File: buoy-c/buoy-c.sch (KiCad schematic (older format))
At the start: 98 parts, among them J1 UJ31-CH-G2-SMT-TR, J10 Conn_01x10_Male, J11 TERM-BLK-2P, J12 TERM-BLK-2P, J13 Conn_01x05_Male, J2 BAT-HLD-001-THM, J3 TERM-BLK-2P, J4 U.FL-R-SMT-1_10_, J5 BH-18650-PC, J6 Conn_01x03_Male, J7 TERM-BLK-2P, J8 Conn_01x03_Male, J9 U.FL-R-SMT-1_10_, Q1 MMBT2222LT1G, Q2 MMBT2222LT1G, Q3 MMBT2222LT1G, U1 ATGM332D-5N31, U10 LTC2954ITS8-1#TRPBF, U2 LTC3113EFE#TRPBF, U3 TP4056, U4 ESP32-WROOM-32D, U5 FT260S-U, U6 TPS61030PWPR, U7 RFM95W-915S2, U8 DS3231M+TRL, U9 ADXL343-EVAL

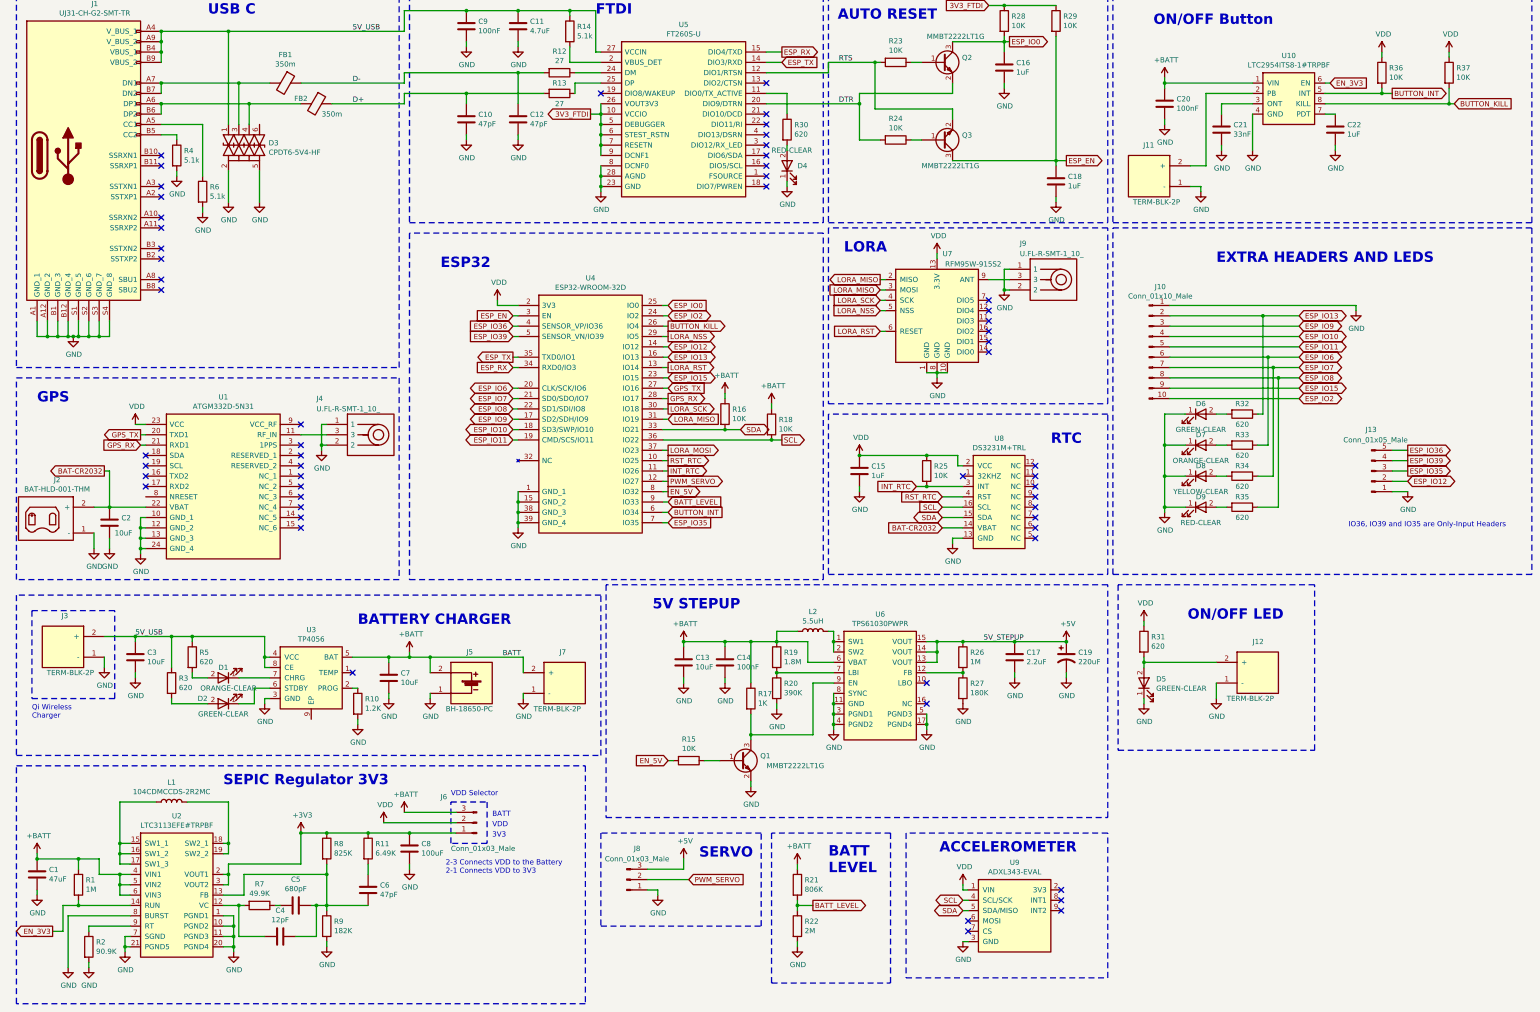
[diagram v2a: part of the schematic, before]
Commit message: Placed components in the PCB
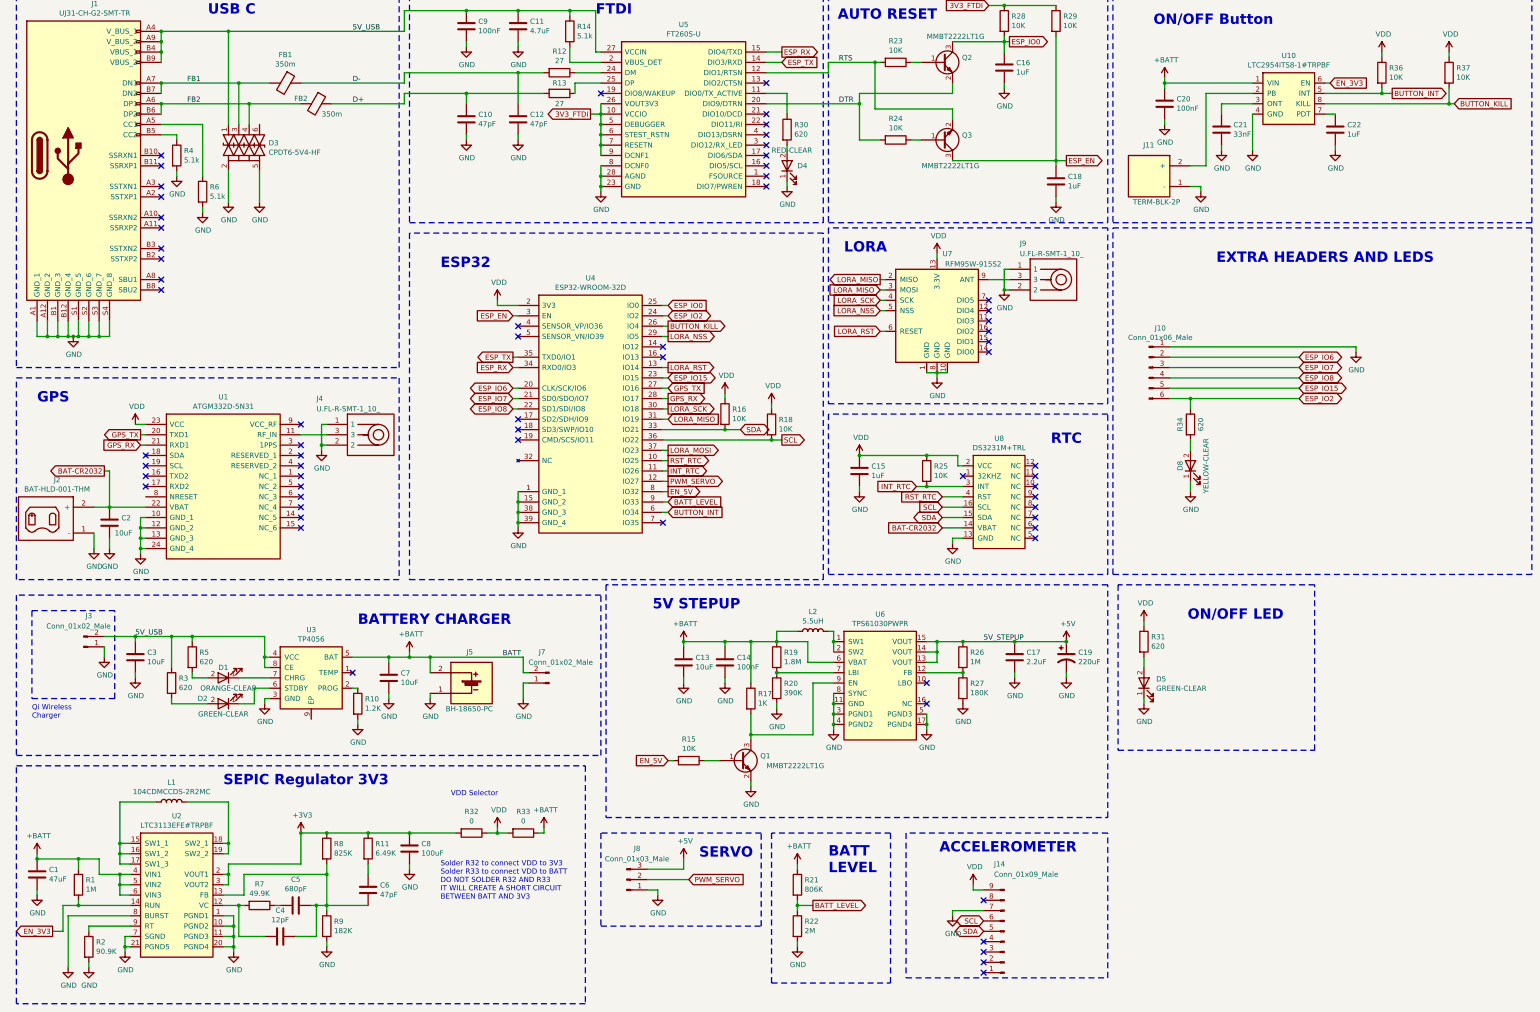
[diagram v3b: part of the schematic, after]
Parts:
- removed D6: GREEN-CLEAR, LED_SMD:LED_0805_2012Metric, symbol LED-GREEN-CLEAR-0805:GREEN-CLEAR
- removed D7: ORANGE-CLEAR, LED_SMD:LED_0805_2012Metric, symbol LED-ORANGE-CLEAR-0805:ORANGE-CLEAR
- removed D9: RED-CLEAR, LED_SMD:LED_0805_2012Metric, symbol LED-RED-CLEAR-0805:RED-CLEAR
- removed J10: Conn_01x10_Male, Connector_PinHeader_2.54mm:PinHeader_1x10_P2.54mm_Vertical, symbol Connector:Conn_01x10_Male
- removed J12, J3, J7: TERM-BLK-2P, TerminalBlock:TerminalBlock_bornier-2_P5.08mm, symbol TERMINAL-BLOCK-2P-508:TERM-BLK-2P
- removed J13: Conn_01x05_Male, Connector_PinHeader_2.54mm:PinHeader_1x05_P2.54mm_Vertical, symbol Connector:Conn_01x05_Male
- removed J6: Conn_01x03_Male, Connector_PinHeader_2.54mm:PinHeader_1x03_P2.54mm_Vertical, symbol Connector:Conn_01x03_Male
- removed R32, R33, R35: 620, Resistor_SMD:R_0805_2012Metric, symbol R-620-0805:620
- removed U9: ADXL343-EVAL, ADXL343-EVAL:ADXL343-EVAL, symbol ADXL343-EVAL:ADXL343-EVAL
- added J10: Conn_01x06_Male, Connector_PinHeader_2.54mm:PinHeader_1x06_P2.54mm_Vertical, symbol Connector:Conn_01x06_Male
- added J14: Conn_01x09_Male, Connector_PinHeader_2.54mm:PinHeader_1x09_P2.54mm_Vertical, symbol Connector:Conn_01x09_Male
- added J3, J7: Conn_01x02_Male, Connector_PinHeader_2.54mm:PinHeader_1x02_P2.54mm_Vertical, symbol Connector:Conn_01x02_Male
- added R32, R33: 0, Resistor_SMD:R_0805_2012Metric, symbol R-0-0805:0
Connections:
- net +3V3: now also R32.2
- net +BATT: now also J7.2 (Pin_2), R33.1; no longer R16.1, R18.1
- net 5V_USB: now also J3.2 (Pin_2)
- net ESP_IO15: now also J10.5 (Pin_5)
- net ESP_IO2: now also R34.1, J10.6 (Pin_6)
- net ESP_IO6: now also J10.2 (Pin_2)
- net ESP_IO7: now also J10.3 (Pin_3); no longer R34.1
- net ESP_IO8: now also J10.4 (Pin_4)
- net GND: now also J10.1 (Pin_1), J14.7 (Pin_7), J3.1 (Pin_1), J7.1 (Pin_1)
- net SCL: now also J14.6 (Pin_6)
- net SDA: now also J14.5 (Pin_5)
- net VDD: now also R16.1, R18.1, J14.9 (Pin_9), R32.1, R33.2
- net FB2: now reaches D3.4, FB2.2, J1.A6 (DP1), J1.B6 (DP2)
- net FB1: now reaches D3.3, FB1.2, J1.A7 (DN1), J1.B7 (DN2)
- net ESP_IO10: no longer names the net of U4.18 (SD3/SWP/IO10)
- net ESP_IO11: no longer names the net of U4.19 (CMD/SCS/IO11)
- net ESP_IO12: no longer names the net of U4.14 (IO12)
- net ESP_IO13: no longer names the net of U4.16 (IO13)
- net ESP_IO35: no longer names the net of U4.7 (IO35)
- net ESP_IO36: no longer names the net of U4.4 (SENSOR_VP/IO36)
- net ESP_IO39: no longer names the net of U4.5 (SENSOR_VN/IO39)
- net ESP_IO9: no longer names the net of U4.17 (SD2/SDH/IO9)
- no-connect marks 57 -> 65
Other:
- note added: "Solder R32 to connect VDD to 3V3\nSolder R33 to connect VDD to BATT\nDO NOT SOLDER R32 AND R33\nIT WILL CREATE A SHORT CIRCUIT\nBETWEEN BATT AND 3V3"
- note removed: "2-3 Connects VDD to the Battery\n2-1 Connects VDD to 3V3"
- note removed: "3V3"
- note removed: "BATT"
- note removed: "IO36, IO39 and IO35 are Only-Input Headers"
- note removed: "VDD"
- moved on the sheet: D8, R34

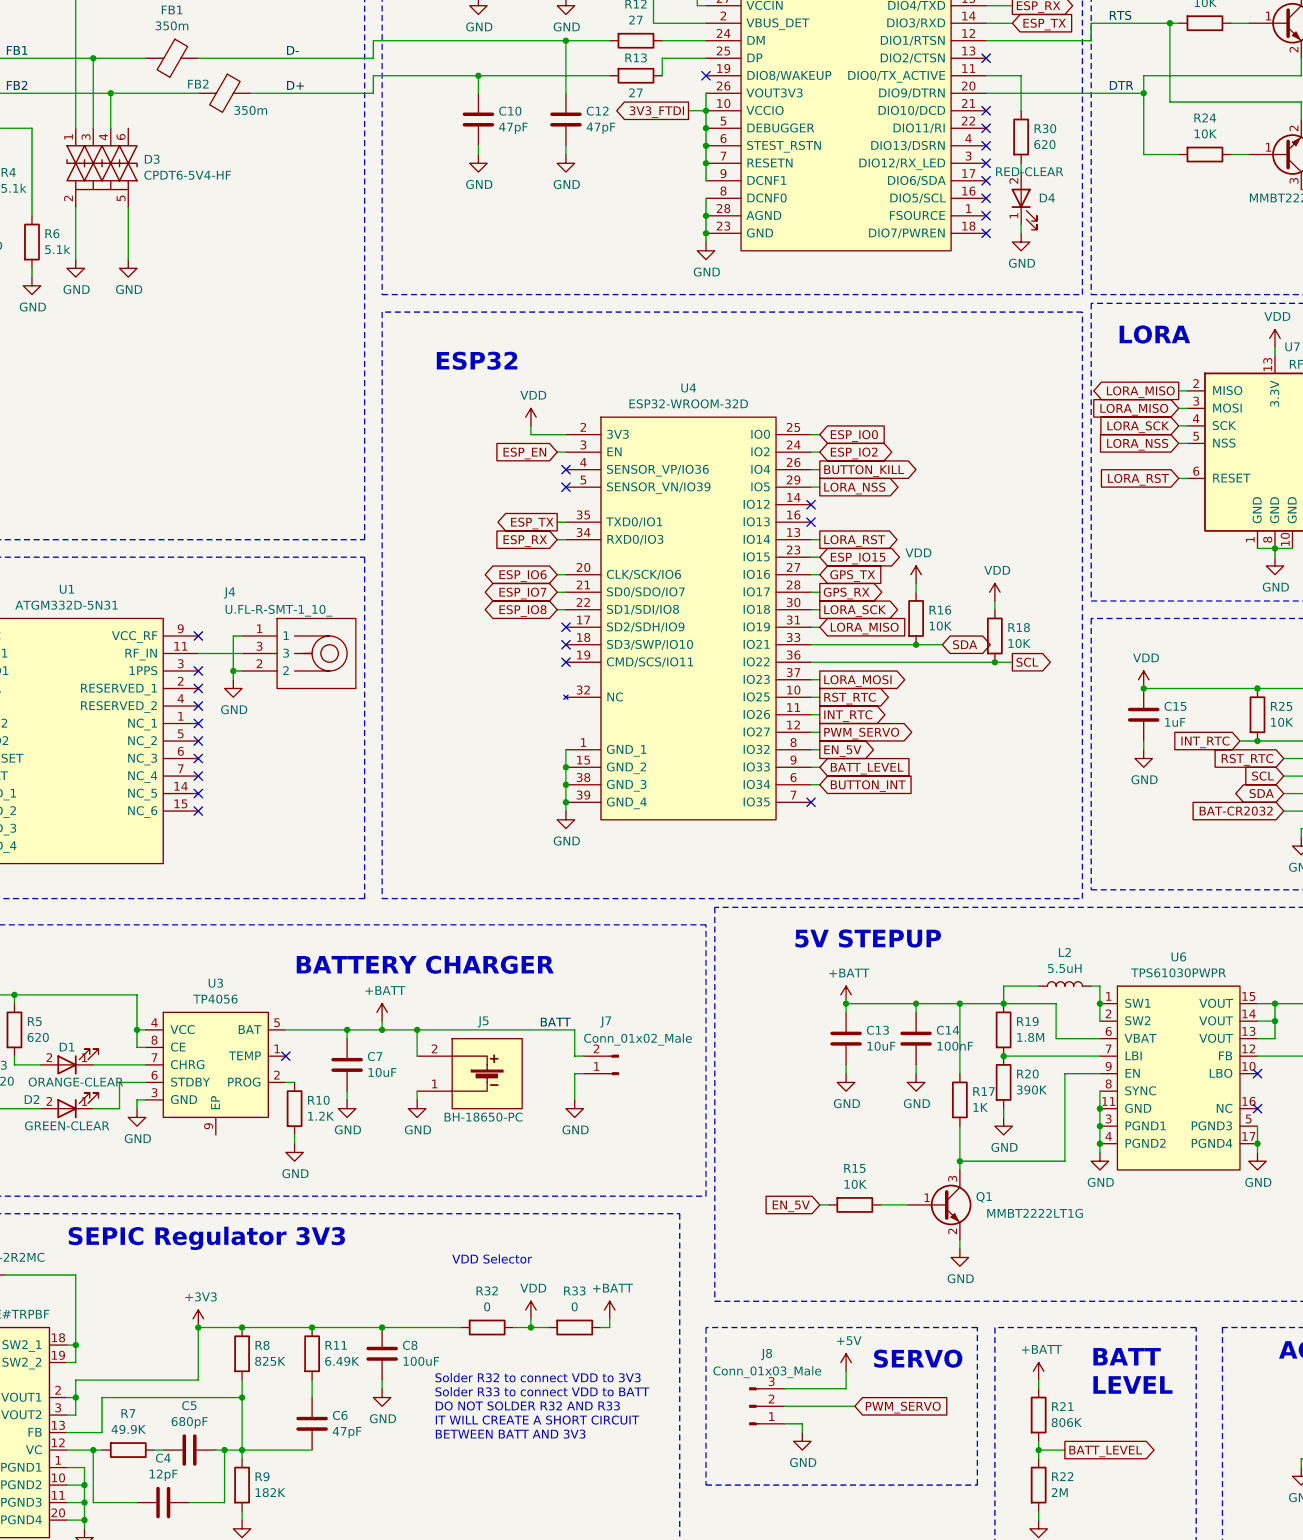
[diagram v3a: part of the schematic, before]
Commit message: Finished routing, solved unconnected
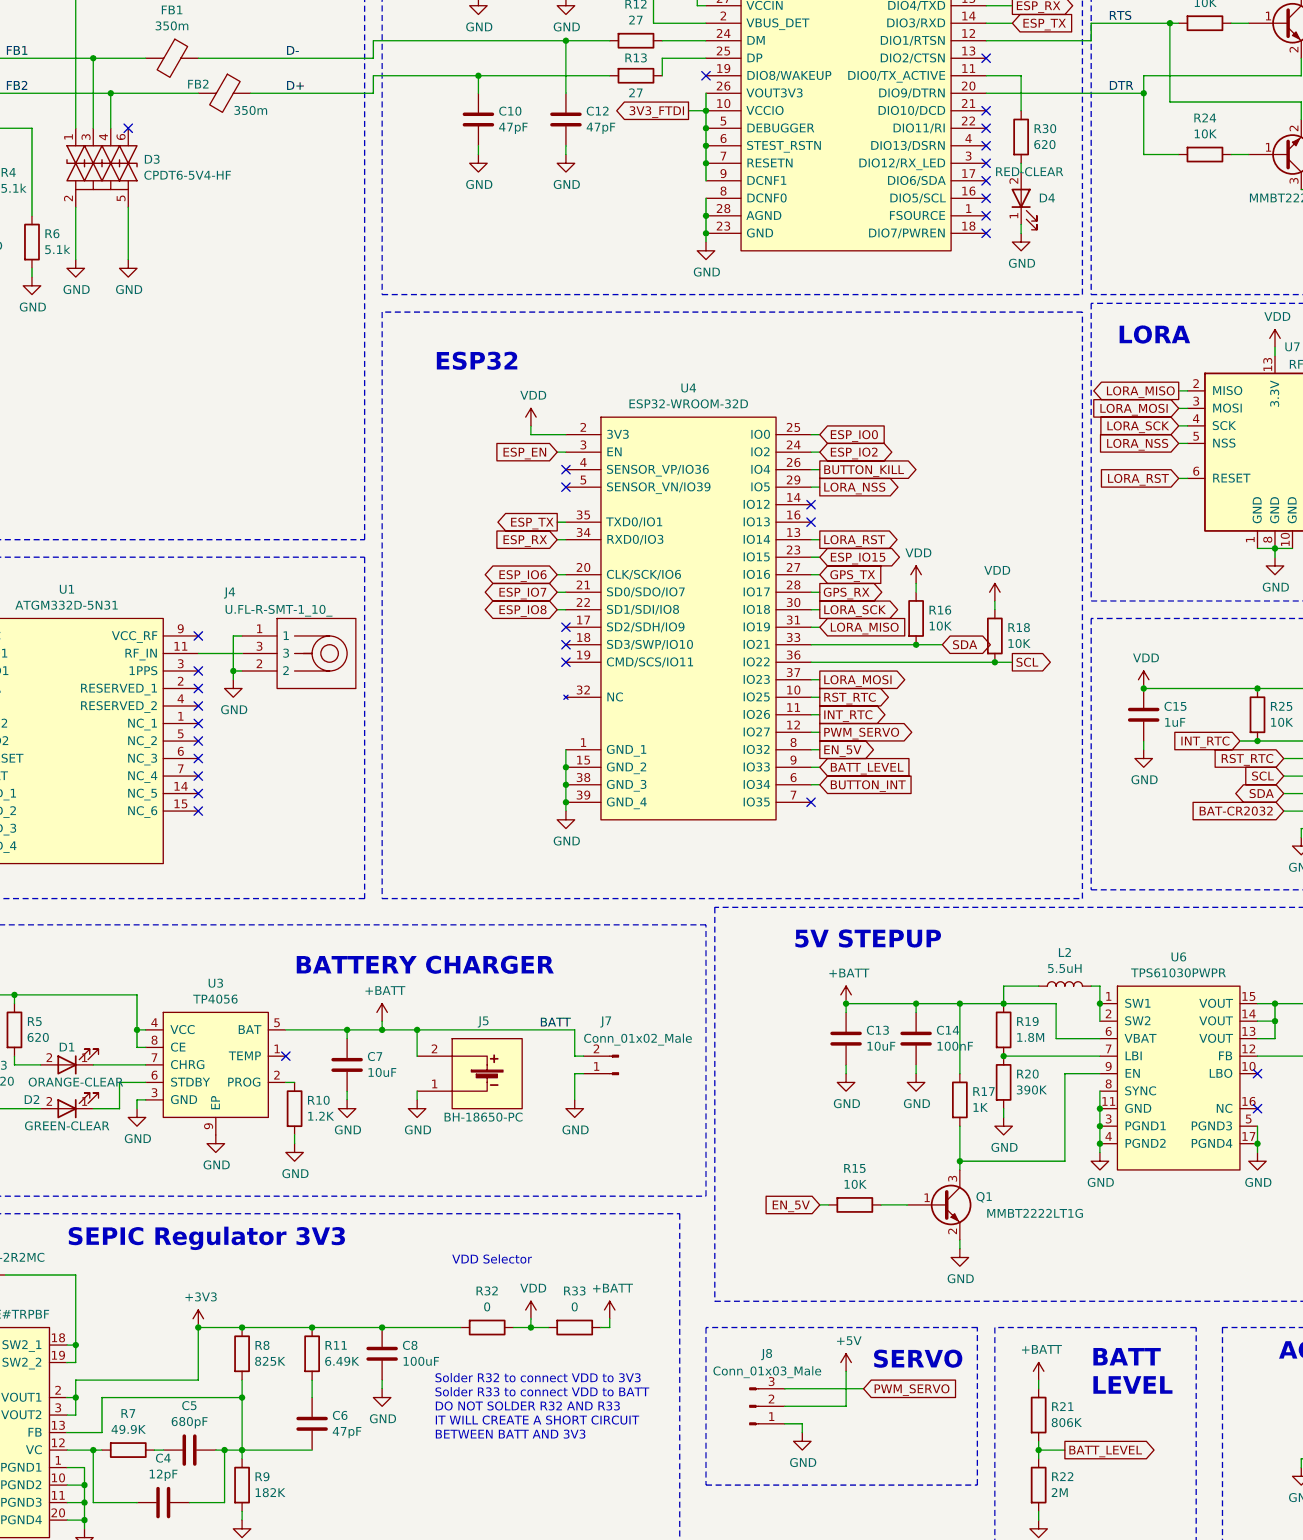
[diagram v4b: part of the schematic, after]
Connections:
- net +5V: now also J8.2 (Pin_2); no longer J8.3 (Pin_3)
- net GND: now also U3.9 (EP)
- net LORA_MISO: no longer U7.3 (MOSI)
- net LORA_MOSI: now also U7.3 (MOSI)
- net PWM_SERVO: now also J8.3 (Pin_3); no longer J8.2 (Pin_2)
- no-connect marks 65 -> 66
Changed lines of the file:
@@
 LORA_MISO
 Text GLabel 9300 3750 0    50   Input ~ 0
-LORA_MISO
+LORA_MOSI
 Text GLabel 9300 3850 0    50   Input ~ 0
 LORA_SCK
@@
 Text Notes 7550 9250 0    100  ~ 20
 SERVO
-Wire Wire Line
-	7450 9450 7050 9450
-Text GLabel 7450 9450 2    50   Input ~ 0
+Text GLabel 7500 9350 2    50   Input ~ 0
 PWM_SERVO
-Wire Wire Line
-	7400 9350 7050 9350
-Wire Wire Line
-	7400 9250 7400 9350
 $Comp
 L power:+5V #PWR0158
@@
 Wire Wire Line
 	6050 9000 6000 9000
+NoConn ~ 3300 2150
+$Comp
+L power:GND #PWR0174
+U 1 1 6132AC93
+P 3800 7900
+F 0 "#PWR0174" H 3800 7650 50  0001 C CNN
+F 1 "GND" H 3805 7727 50  0000 C CNN
+F 2 "" H 3800 7900 50  0001 C CNN
+F 3 "" H 3800 7900 50  0001 C CNN
+	1    3800 7900
+	1    0    0    -1
+$EndComp
+Wire Wire Line
+	7500 9350 7050 9350
+Wire Wire Line
+	7400 9250 7400 9450
+Wire Wire Line
+	7400 9450 7050 9450
 $EndSCHEMATC
